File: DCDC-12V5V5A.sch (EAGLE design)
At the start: 37 parts, among them CN2 2828XX-2282834-2, CN3 2828XX-2282834-2, Q10 NMOSFET, Q9 NMOSFET, U1 LM3150MHX/NOPB

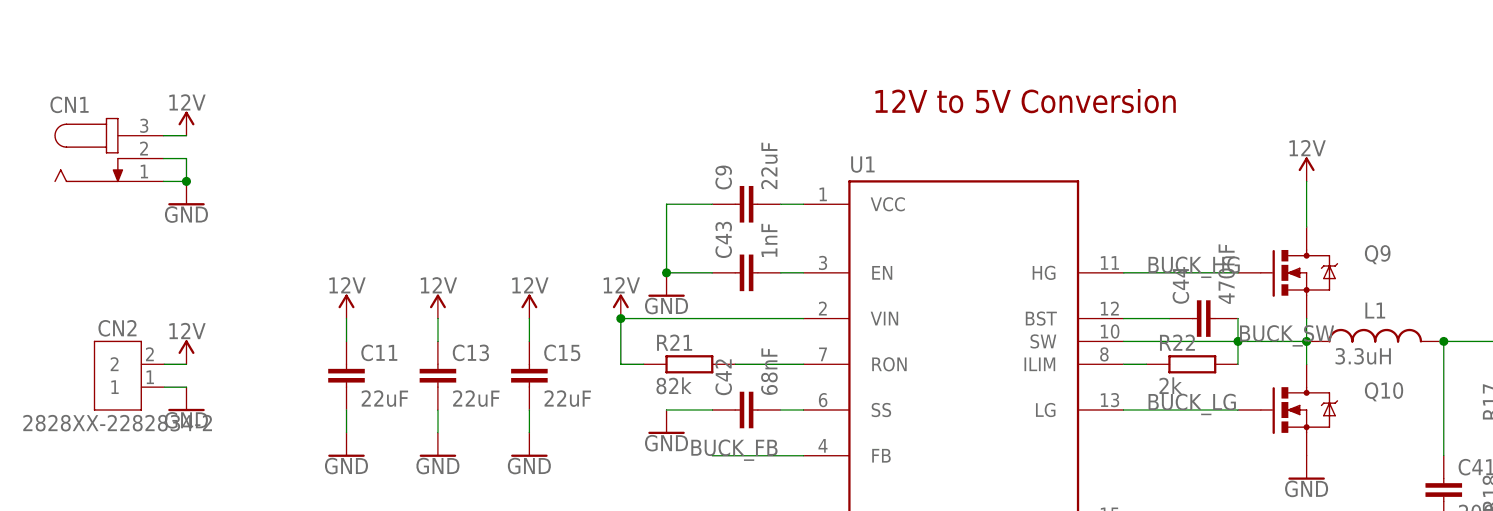
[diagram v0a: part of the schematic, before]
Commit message: Renamed 12V line to Vin. Generated CAM files.
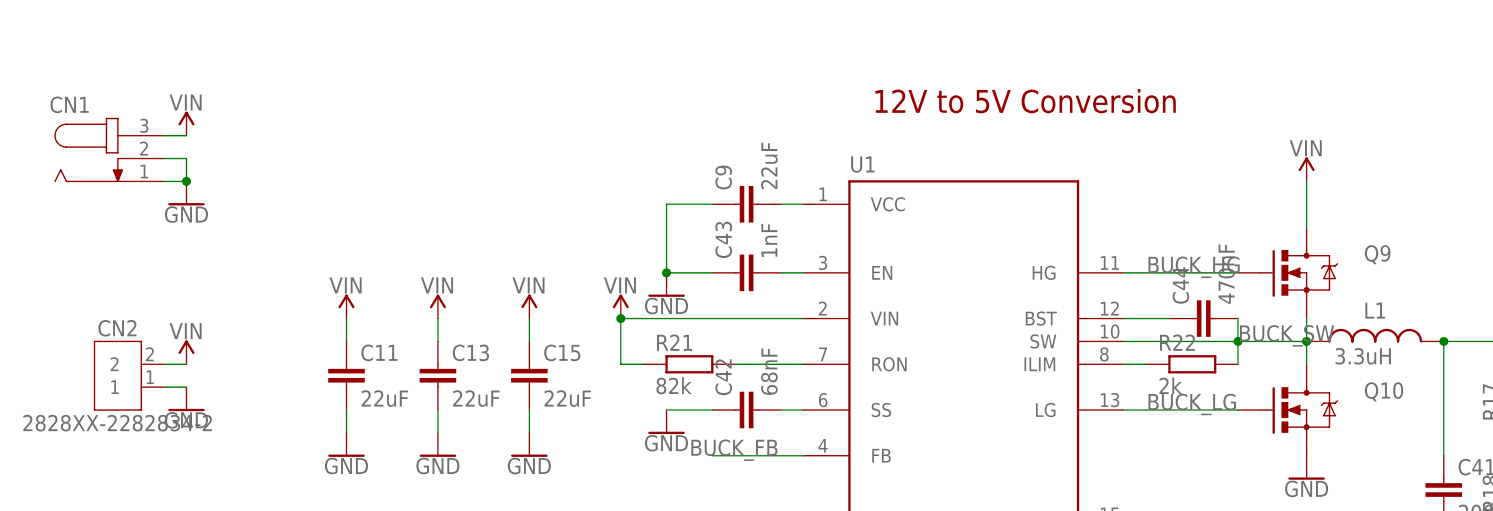
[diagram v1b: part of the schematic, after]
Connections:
- net 12V renamed VIN
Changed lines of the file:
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@@
 <part name="Q9" library="BeagleBone_Blue_R3" library_urn="urn:adsk.eagle:library:5828899" deviceset="MOSFET-NCHANNEL" device="FDD8780" package3d_urn="urn:adsk.eagle:package:5829549/1" value="NMOSFET"/>
 <part name="Q10" library="BeagleBone_Blue_R3" library_urn="urn:adsk.eagle:library:5828899" deviceset="MOSFET-NCHANNEL" device="FDD8780" package3d_urn="urn:adsk.eagle:package:5829549/1" value="NMOSFET"/>
-<part name="SUPPLY44" library="SparkFun-PowerSymbols" library_urn="urn:adsk.eagle:library:530" deviceset="12V" device=""/>
+<part name="SUPPLY44" library="SparkFun-PowerSymbols" library_urn="urn:adsk.eagle:library:530" deviceset="VIN" device=""/>
 <part name="GND51" library="SparkFun-PowerSymbols" library_urn="urn:adsk.eagle:library:530" deviceset="GND" device=""/>
 <part name="L1" library="Wurth_Automotive_WE-CHSA" library_urn="urn:adsk.eagle:library:14076700" deviceset="WE-CHSA_1011" device="" package3d_urn="urn:adsk.eagle:package:13154812/4" technology="_7843330330" value="3.3uH"/>
 <part name="SUPPLY45" library="SparkFun-PowerSymbols" library_urn="urn:adsk.eagle:library:530" deviceset="5V" device=""/>
 <part name="GND52" library="SparkFun-PowerSymbols" library_urn="urn:adsk.eagle:library:530" deviceset="GND" device=""/>
-<part name="SUPPLY46" library="SparkFun-PowerSymbols" library_urn="urn:adsk.eagle:library:530" deviceset="12V" device=""/>
+<part name="SUPPLY46" library="SparkFun-PowerSymbols" library_urn="urn:adsk.eagle:library:530" deviceset="VIN" device=""/>
 <part name="R17" library="rcl" library_urn="urn:adsk.eagle:library:334" deviceset="R-EU_" device="R0603" package3d_urn="urn:adsk.eagle:package:23555/3" value="68k"/>
 <part name="R18" library="rcl" library_urn="urn:adsk.eagle:library:334" deviceset="R-EU_" device="R0603" package3d_urn="urn:adsk.eagle:package:23555/3" value="3k"/>
@@
 <part name="R22" library="rcl" library_urn="urn:adsk.eagle:library:334" deviceset="R-EU_" device="R0603" package3d_urn="urn:adsk.eagle:package:23555/3" value="2k"/>
 <part name="C44" library="rcl" library_urn="urn:adsk.eagle:library:334" deviceset="C-EU" device="C0603K" package3d_urn="urn:adsk.eagle:package:23680/2" value="470nF"/>
-<part name="SUPPLY2" library="SparkFun-PowerSymbols" library_urn="urn:adsk.eagle:library:530" deviceset="12V" device=""/>
-<part name="SUPPLY3" library="SparkFun-PowerSymbols" library_urn="urn:adsk.eagle:library:530" deviceset="12V" device=""/>
-<part name="SUPPLY5" library="SparkFun-PowerSymbols" library_urn="urn:adsk.eagle:library:530" deviceset="12V" device=""/>
+<part name="SUPPLY2" library="SparkFun-PowerSymbols" library_urn="urn:adsk.eagle:library:530" deviceset="VIN" device=""/>
+<part name="SUPPLY3" library="SparkFun-PowerSymbols" library_urn="urn:adsk.eagle:library:530" deviceset="VIN" device=""/>
+<part name="SUPPLY5" library="SparkFun-PowerSymbols" library_urn="urn:adsk.eagle:library:530" deviceset="VIN" device=""/>
 <part name="SUPPLY8" library="SparkFun-PowerSymbols" library_urn="urn:adsk.eagle:library:530" deviceset="5V" device=""/>
 <part name="SUPPLY47" library="SparkFun-PowerSymbols" library_urn="urn:adsk.eagle:library:530" deviceset="5V" device=""/>
@@
 <part name="GND1" library="SparkFun-PowerSymbols" library_urn="urn:adsk.eagle:library:530" deviceset="GND" device=""/>
 <part name="GND2" library="SparkFun-PowerSymbols" library_urn="urn:adsk.eagle:library:530" deviceset="GND" device=""/>
-<part name="SUPPLY1" library="SparkFun-PowerSymbols" library_urn="urn:adsk.eagle:library:530" deviceset="12V" device=""/>
-<part name="SUPPLY4" library="SparkFun-PowerSymbols" library_urn="urn:adsk.eagle:library:530" deviceset="12V" device=""/>
+<part name="SUPPLY1" library="SparkFun-PowerSymbols" library_urn="urn:adsk.eagle:library:530" deviceset="VIN" device=""/>
+<part name="SUPPLY4" library="SparkFun-PowerSymbols" library_urn="urn:adsk.eagle:library:530" deviceset="VIN" device=""/>
 <part name="GND3" library="SparkFun-PowerSymbols" library_urn="urn:adsk.eagle:library:530" deviceset="GND" device=""/>
 <part name="SUPPLY6" library="SparkFun-PowerSymbols" library_urn="urn:adsk.eagle:library:530" deviceset="5V" device=""/>
@@
 </busses>
 <nets>
-<net name="12V" class="0">
+<net name="VIN" class="0">
 <segment>
 <pinref part="Q9" gate="G$1" pin="D"/>
 <wire x1="154.94" y1="124.46" x2="154.94" y2="129.54" width="0.1524" layer="91"/>
-<pinref part="SUPPLY44" gate="G$1" pin="12V"/>
+<pinref part="SUPPLY44" gate="G$1" pin="VIN"/>
 </segment>
 <segment>
 <pinref part="U1" gate="G$1" pin="VIN"/>
 <wire x1="99.06" y1="114.3" x2="78.74" y2="114.3" width="0.1524" layer="91"/>
-<pinref part="SUPPLY46" gate="G$1" pin="12V"/>
+<pinref part="SUPPLY46" gate="G$1" pin="VIN"/>
 <pinref part="R21" gate="G$1" pin="1"/>
 <wire x1="81.28" y1="109.22" x2="78.74" y2="109.22" width="0.1524" layer="91"/>
@@
 <pinref part="C15" gate="G$1" pin="1"/>
 <wire x1="68.58" y1="111.76" x2="68.58" y2="114.3" width="0.1524" layer="91"/>
-<pinref part="SUPPLY2" gate="G$1" pin="12V"/>
+<pinref part="SUPPLY2" gate="G$1" pin="VIN"/>
 </segment>
 <segment>
 <pinref part="C13" gate="G$1" pin="1"/>
 <wire x1="58.42" y1="111.76" x2="58.42" y2="114.3" width="0.1524" layer="91"/>
-<pinref part="SUPPLY3" gate="G$1" pin="12V"/>
+<pinref part="SUPPLY3" gate="G$1" pin="VIN"/>
 </segment>
 <segment>
 <pinref part="C11" gate="G$1" pin="1"/>
 <wire x1="48.26" y1="111.76" x2="48.26" y2="114.3" width="0.1524" layer="91"/>
-<pinref part="SUPPLY5" gate="G$1" pin="12V"/>
-</segment>
-<segment>
-<pinref part="SUPPLY4" gate="G$1" pin="12V"/>
+<pinref part="SUPPLY5" gate="G$1" pin="VIN"/>
+</segment>
+<segment>
+<pinref part="SUPPLY4" gate="G$1" pin="VIN"/>
 <pinref part="CN2" gate="G$1" pin="2"/>
 <wire x1="30.48" y1="109.22" x2="28.01" y2="109.22" width="0.1524" layer="91"/>
@@
 <segment>
 <pinref part="CN1" gate="G$1" pin="3"/>
-<pinref part="SUPPLY1" gate="G$1" pin="12V"/>
+<pinref part="SUPPLY1" gate="G$1" pin="VIN"/>
 <wire x1="27.94" y1="134.62" x2="30.48" y2="134.62" width="0.1524" layer="91"/>
 </segment>

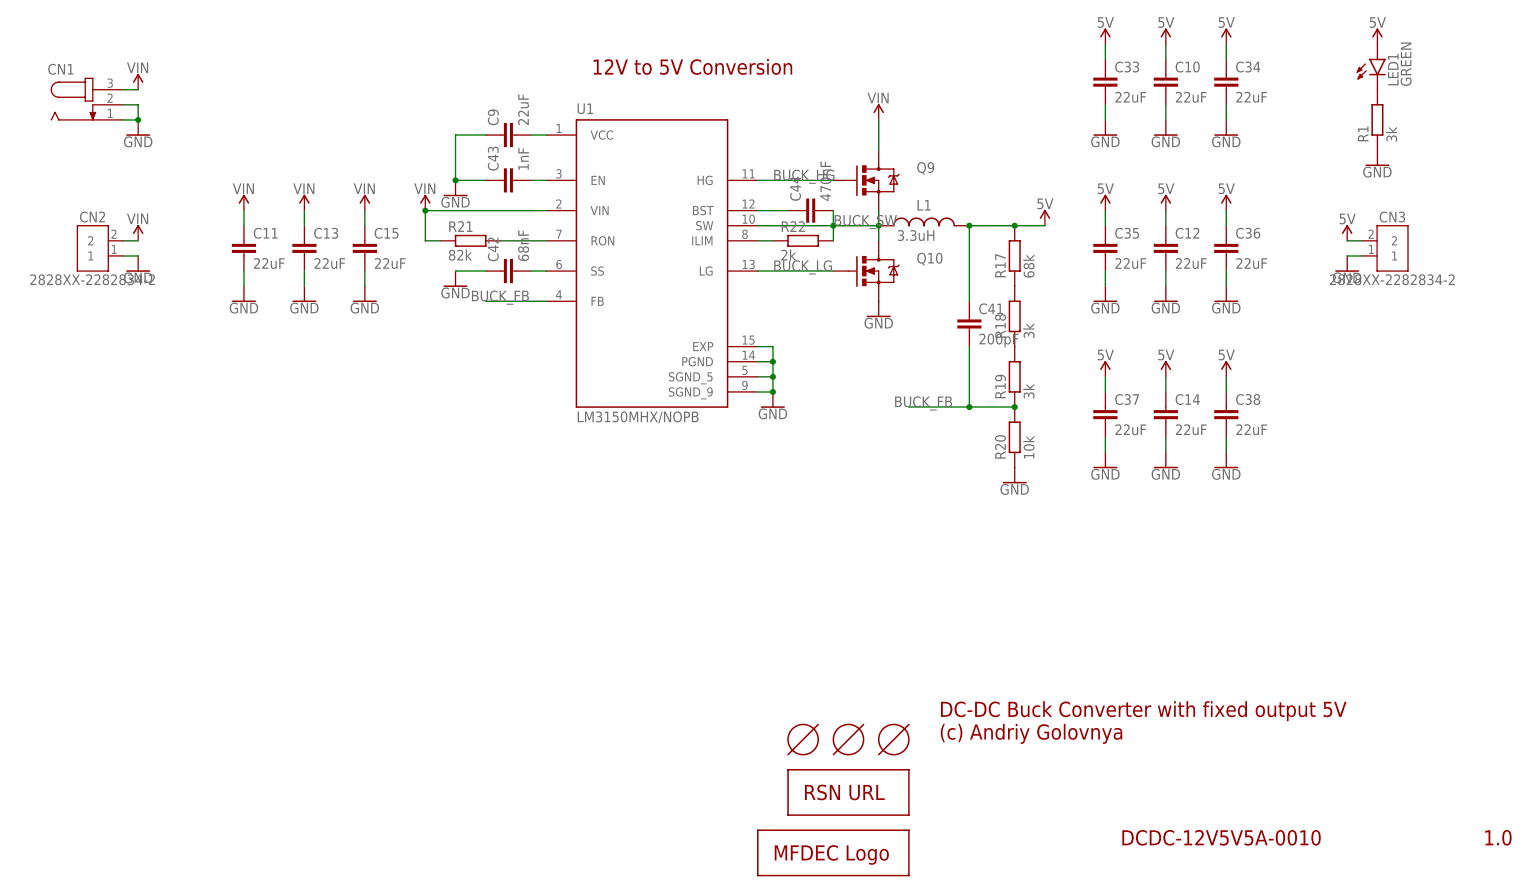
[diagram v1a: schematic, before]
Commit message: Made new layout of DC-DC board. Improved XLS calculator. Generated CAM files. Generated BoM and PnP files. Generated PNG preview. Generated PDF schematics.
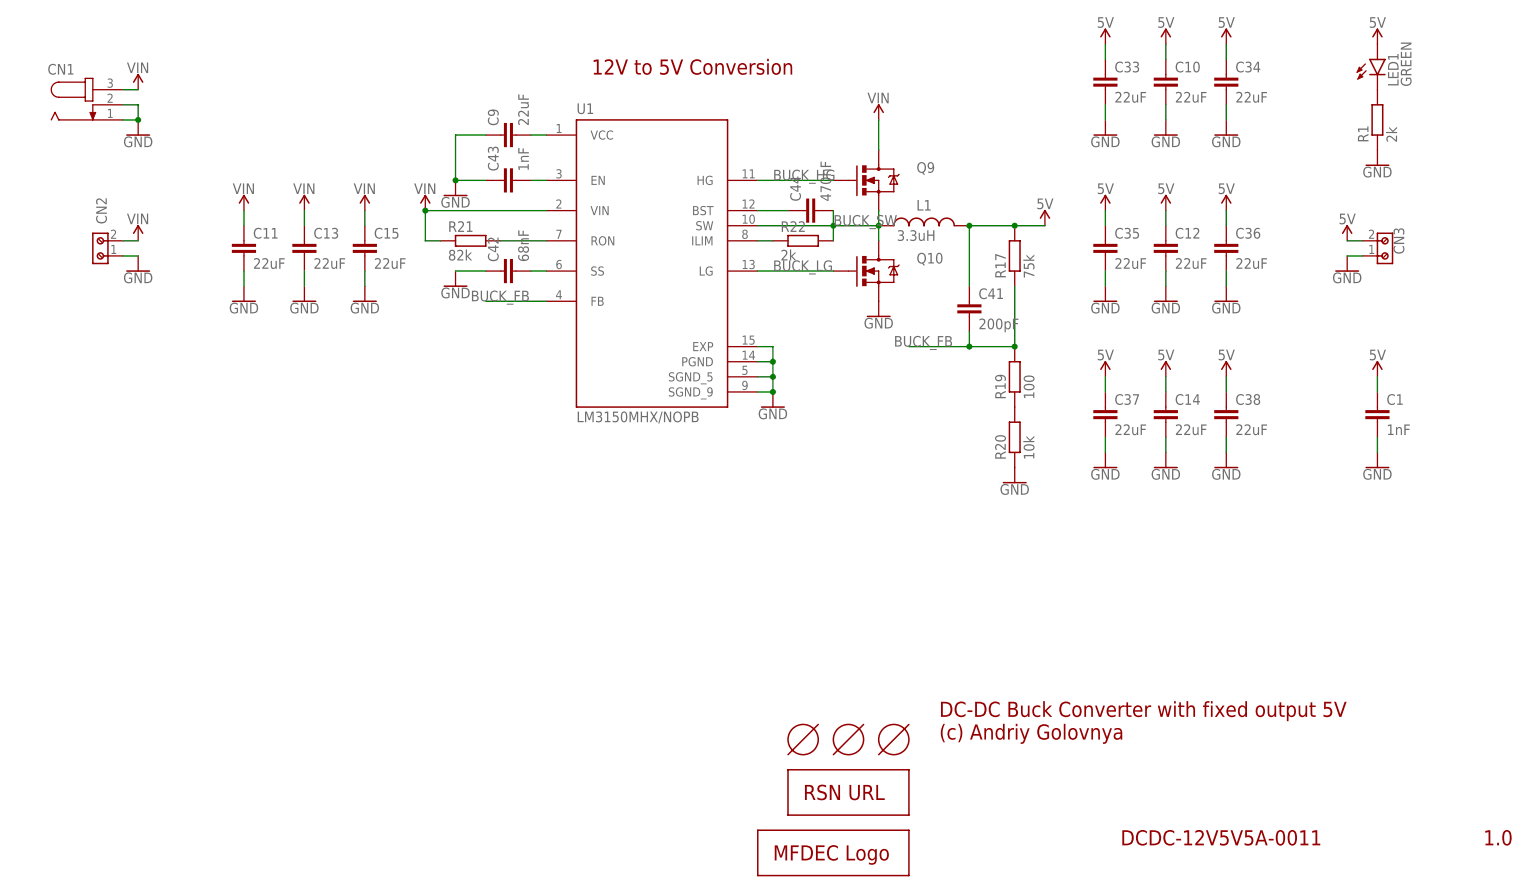
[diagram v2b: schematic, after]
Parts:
- removed R18: 3k, rcl:R-EU_R0603
- added C1: 1nF, rcl:C-EUC0603K
- CN2, CN3: value 2828XX-2282834-2 -> (none); device Connector:2828XX-2282834-2 -> Wurth_Connectors_WR-TBL Rising Cage Clamp:691213510002
- R1: value 3k -> 2k
- R17: value 68k -> 75k
- R19: value 3k -> 100
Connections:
- net N$16 renamed BUCK_SS
- net N$18 renamed BUCK_EN
- net N$19 renamed BUCK_VCC
- net N$21 renamed BUCK_RON
- net N$23 renamed BUCK_BST
- net N$8 renamed BUCK_ILIM
- removed net N$13: R18.1, R19.2
- removed net N$9: R17.1, R18.2
- new net N$2: R19.1, R20.2
- net 5V: now also C1.1
- net BUCK_FB: now also R17.1, R19.2; no longer R19.1, R20.2
- net GND: now also C1.2
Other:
- note added: "DCDC-12V5V5A-0011"
- note removed: "DCDC-12V5V5A-0010"
- moved on the sheet: C41

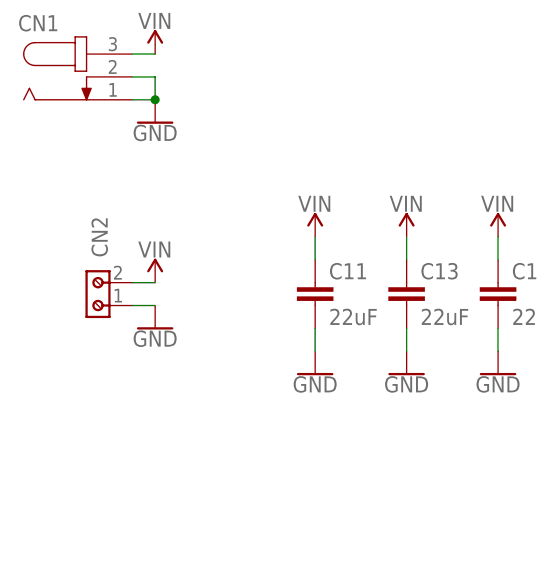
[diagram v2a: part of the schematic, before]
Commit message: Improved layout of DC-DC board. Rotated input terminal. Improved XLS calculator. Generated CAM files. Generated BoM and PnP files. Generated PNG preview. Generated PDF schematics.
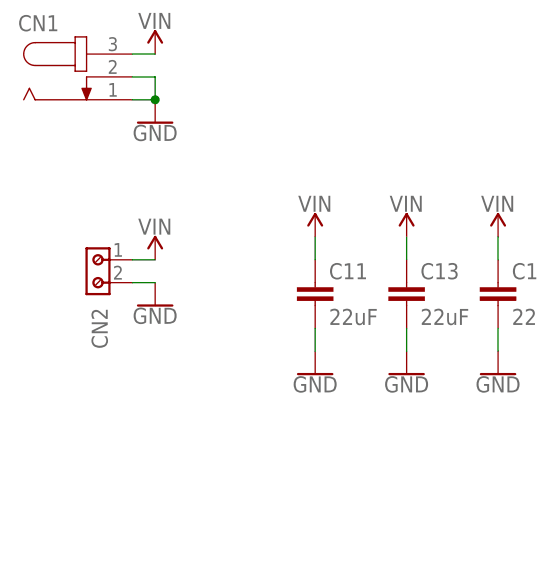
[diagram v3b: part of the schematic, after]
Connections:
- net GND: now also CN2.2; no longer CN2.1
- net VIN: now also CN2.1; no longer CN2.2
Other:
- moved on the sheet: CN2
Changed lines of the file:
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@@
 <part name="CN2" library="Wurth_Connectors_WR-TBL Rising Cage Clamp" library_urn="urn:adsk.eagle:library:16280519" deviceset="691213510002" device="" package3d_urn="urn:adsk.eagle:package:16248575/2"/>
 <part name="CN3" library="Wurth_Connectors_WR-TBL Rising Cage Clamp" library_urn="urn:adsk.eagle:library:16280519" deviceset="691213510002" device="" package3d_urn="urn:adsk.eagle:package:16248575/2"/>
-<part name="GND1" library="SparkFun-PowerSymbols" library_urn="urn:adsk.eagle:library:530" deviceset="GND" device=""/>
 <part name="GND2" library="SparkFun-PowerSymbols" library_urn="urn:adsk.eagle:library:530" deviceset="GND" device=""/>
 <part name="SUPPLY1" library="SparkFun-PowerSymbols" library_urn="urn:adsk.eagle:library:530" deviceset="VIN" device=""/>
-<part name="SUPPLY4" library="SparkFun-PowerSymbols" library_urn="urn:adsk.eagle:library:530" deviceset="VIN" device=""/>
 <part name="GND3" library="SparkFun-PowerSymbols" library_urn="urn:adsk.eagle:library:530" deviceset="GND" device=""/>
 <part name="SUPPLY6" library="SparkFun-PowerSymbols" library_urn="urn:adsk.eagle:library:530" deviceset="5V" device=""/>
@@
 <part name="SUPPLY9" library="SparkFun-PowerSymbols" library_urn="urn:adsk.eagle:library:530" deviceset="5V" device=""/>
 <part name="GND5" library="SparkFun-PowerSymbols" library_urn="urn:adsk.eagle:library:530" deviceset="GND" device=""/>
+<part name="SUPPLY4" library="SparkFun-PowerSymbols" library_urn="urn:adsk.eagle:library:530" deviceset="VIN" device=""/>
+<part name="GND1" library="SparkFun-PowerSymbols" library_urn="urn:adsk.eagle:library:530" deviceset="GND" device=""/>
 </parts>
 <sheets>
@@
 <attribute name="VALUE" x="15.24" y="127" size="1.778" layer="96"/>
 </instance>
-<instance part="CN2" gate="G$1" x="22.86" y="109.22" smashed="yes" rot="R90">
-<attribute name="NAME" x="24.32" y="114.3" size="1.778" layer="95" rot="R90" align="center"/>
-<attribute name="VALUE" x="16.32" y="109.22" size="1.778" layer="95" rot="R90" align="center"/>
+<instance part="CN2" gate="G$1" x="22.86" y="109.22" smashed="yes" rot="MR270">
+<attribute name="NAME" x="24.32" y="104.14" size="1.778" layer="95" rot="MR270" align="center"/>
+<attribute name="VALUE" x="16.32" y="109.22" size="1.778" layer="95" rot="MR270" align="center"/>
 </instance>
 <instance part="CN3" gate="G$1" x="241.3" y="109.22" smashed="yes" rot="MR90">
@@
 <attribute name="VALUE" x="247.84" y="109.22" size="1.778" layer="95" rot="MR90" align="center"/>
 </instance>
-<instance part="GND1" gate="1" x="30.48" y="104.14" smashed="yes">
-<attribute name="VALUE" x="30.48" y="103.886" size="1.778" layer="96" align="top-center"/>
-</instance>
 <instance part="GND2" gate="1" x="30.48" y="127" smashed="yes">
 <attribute name="VALUE" x="30.48" y="126.746" size="1.778" layer="96" align="top-center"/>
@@
 <instance part="SUPPLY1" gate="G$1" x="30.48" y="134.62" smashed="yes">
 <attribute name="VALUE" x="30.48" y="137.414" size="1.778" layer="96" align="bottom-center"/>
-</instance>
-<instance part="SUPPLY4" gate="G$1" x="30.48" y="109.22" smashed="yes">
-<attribute name="VALUE" x="30.48" y="112.014" size="1.778" layer="96" align="bottom-center"/>
 </instance>
 <instance part="GND3" gate="1" x="233.68" y="104.14" smashed="yes">
@@
 <instance part="GND5" gate="1" x="238.76" y="71.12" smashed="yes">
 <attribute name="VALUE" x="238.76" y="70.866" size="1.778" layer="96" align="top-center"/>
+</instance>
+<instance part="SUPPLY4" gate="G$1" x="30.48" y="111.76" smashed="yes">
+<attribute name="VALUE" x="30.48" y="114.554" size="1.778" layer="96" align="bottom-center"/>
+</instance>
+<instance part="GND1" gate="1" x="30.48" y="106.68" smashed="yes">
+<attribute name="VALUE" x="30.48" y="106.426" size="1.778" layer="96" align="top-center"/>
 </instance>
 </instances>
@@
 </segment>
 <segment>
-<pinref part="SUPPLY4" gate="G$1" pin="VIN"/>
-<pinref part="CN2" gate="G$1" pin="2"/>
-<wire x1="30.48" y1="109.22" x2="27.94" y2="109.22" width="0.1524" layer="91"/>
-</segment>
-<segment>
 <pinref part="CN1" gate="G$1" pin="3"/>
 <pinref part="SUPPLY1" gate="G$1" pin="VIN"/>
 <wire x1="27.94" y1="134.62" x2="30.48" y2="134.62" width="0.1524" layer="91"/>
+</segment>
+<segment>
+<pinref part="CN2" gate="G$1" pin="1"/>
+<wire x1="27.94" y1="111.76" x2="30.48" y2="111.76" width="0.1524" layer="91"/>
+<pinref part="SUPPLY4" gate="G$1" pin="VIN"/>
 </segment>
 </net>
@@
 </segment>
 <segment>
-<pinref part="GND1" gate="1" pin="GND"/>
-<pinref part="CN2" gate="G$1" pin="1"/>
-<wire x1="30.48" y1="106.68" x2="27.94" y2="106.68" width="0.1524" layer="91"/>
-</segment>
-<segment>
 <pinref part="CN1" gate="G$1" pin="1"/>
 <pinref part="GND2" gate="1" pin="GND"/>
@@
 <wire x1="238.76" y1="73.66" x2="238.76" y2="76.2" width="0.1524" layer="91"/>
 </segment>
+<segment>
+<pinref part="CN2" gate="G$1" pin="2"/>
+<wire x1="27.94" y1="109.22" x2="30.48" y2="109.22" width="0.1524" layer="91"/>
+<pinref part="GND1" gate="1" pin="GND"/>
+</segment>
 </net>
